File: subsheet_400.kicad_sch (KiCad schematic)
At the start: 24 parts, among them U400 STE_GSTMCU_PHY

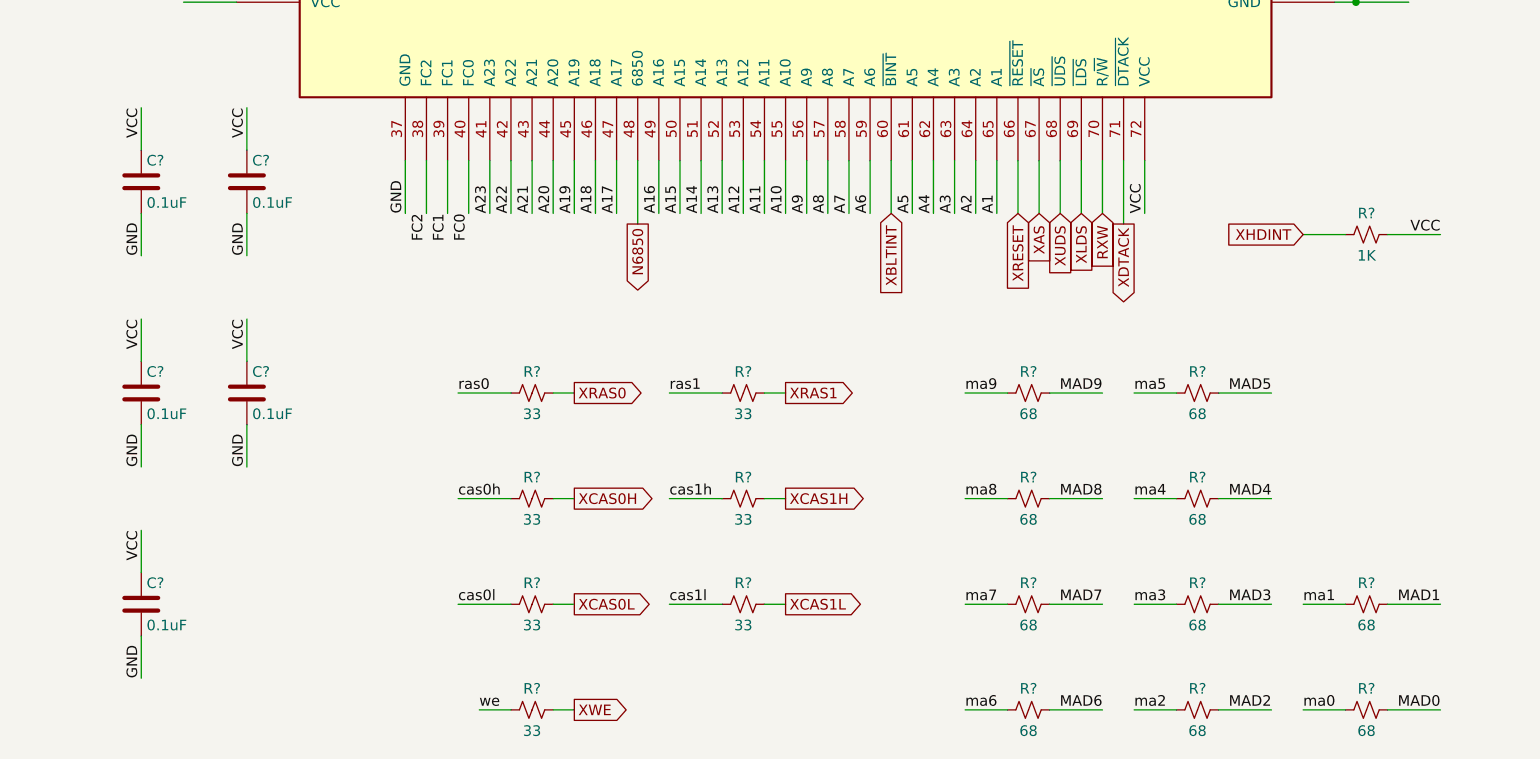
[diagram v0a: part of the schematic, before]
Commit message: Resolves #3 : [schematic] annotate video port with signal name
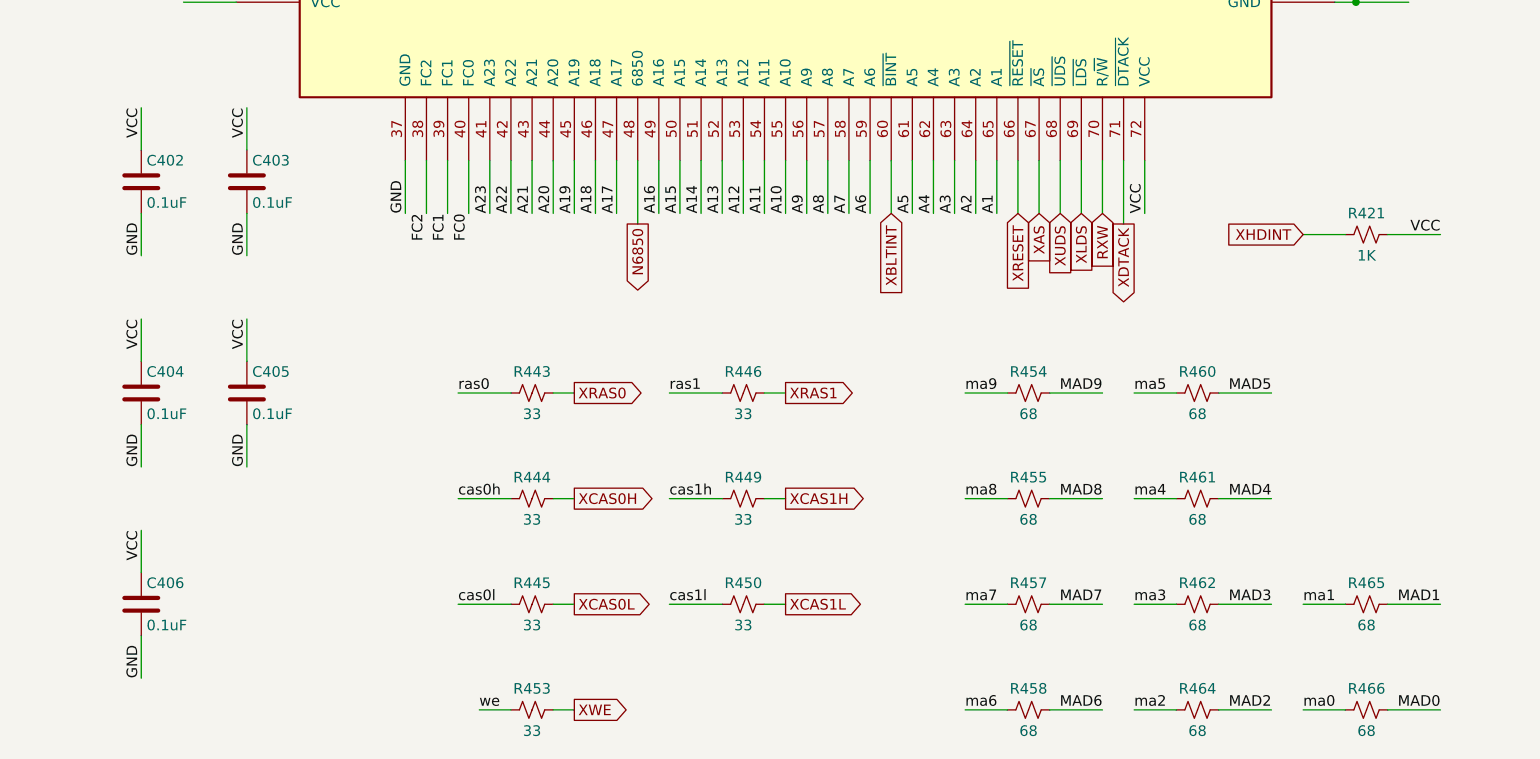
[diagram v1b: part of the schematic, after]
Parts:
- gave numbers to parts that had none: 23
